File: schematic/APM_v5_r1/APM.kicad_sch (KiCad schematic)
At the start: 27 parts, among them J10 Conn_02x17_Counter_Clockwise, J13 Conn_01x06, J14 POT_FFC, J18 CTRL_FFC, J2 CAN, J20 FPGA_UART, J4 LCD_display, J6 Conn_02x10_Counter_Clockwise, J8 Conn_02x15_Counter_Clockwise, J9 Conn_02x08_Counter_Clockwise

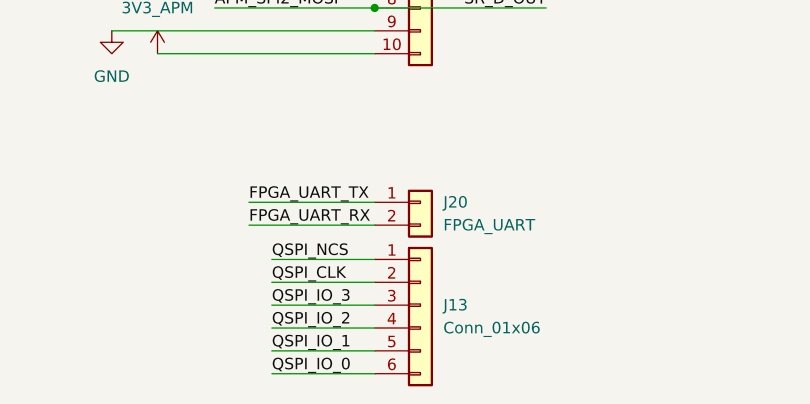
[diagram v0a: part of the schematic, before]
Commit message: figuring out FFC traces next
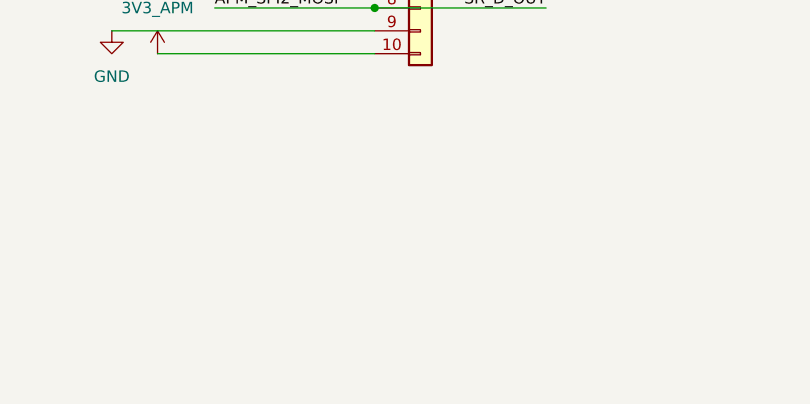
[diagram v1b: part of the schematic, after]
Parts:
- removed J13: Conn_01x06, Connector_PinHeader_2.54mm:PinHeader_1x06_P2.54mm_Vertical, symbol Connector_Generic:Conn_01x06
- removed J20: FPGA_UART, Connector_PinHeader_2.54mm:PinHeader_1x02_P2.54mm_Vertical, symbol Connector_Generic:Conn_01x02

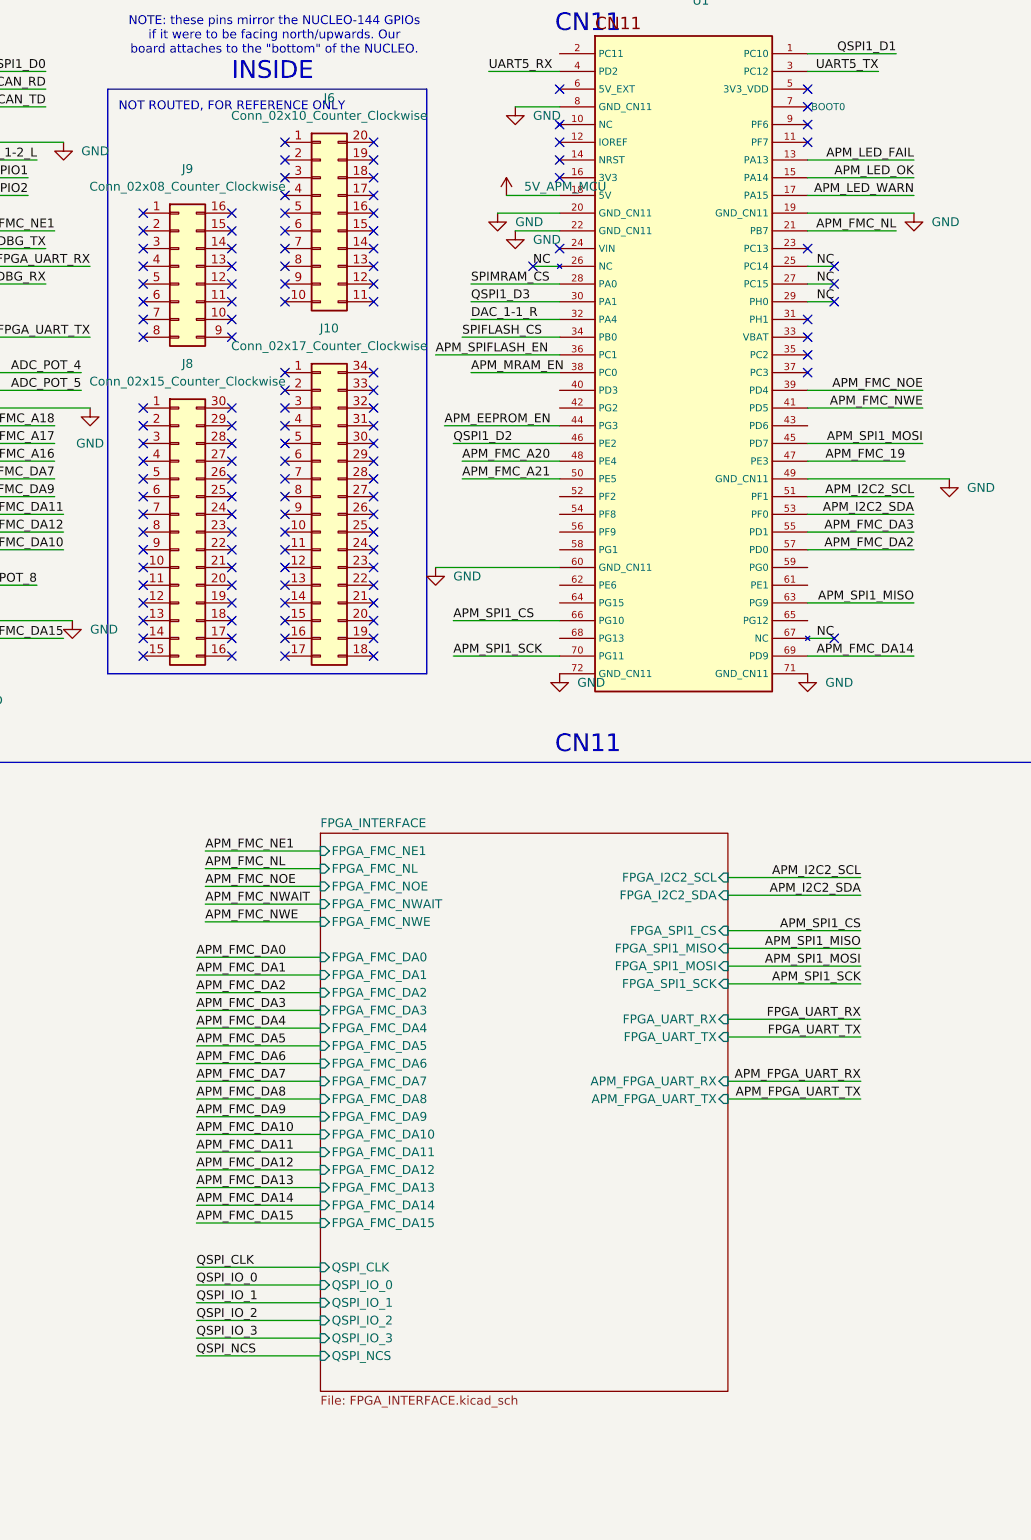
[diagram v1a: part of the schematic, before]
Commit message: getting ACM and APM schematics put together. tool for FMC pin mapping verif
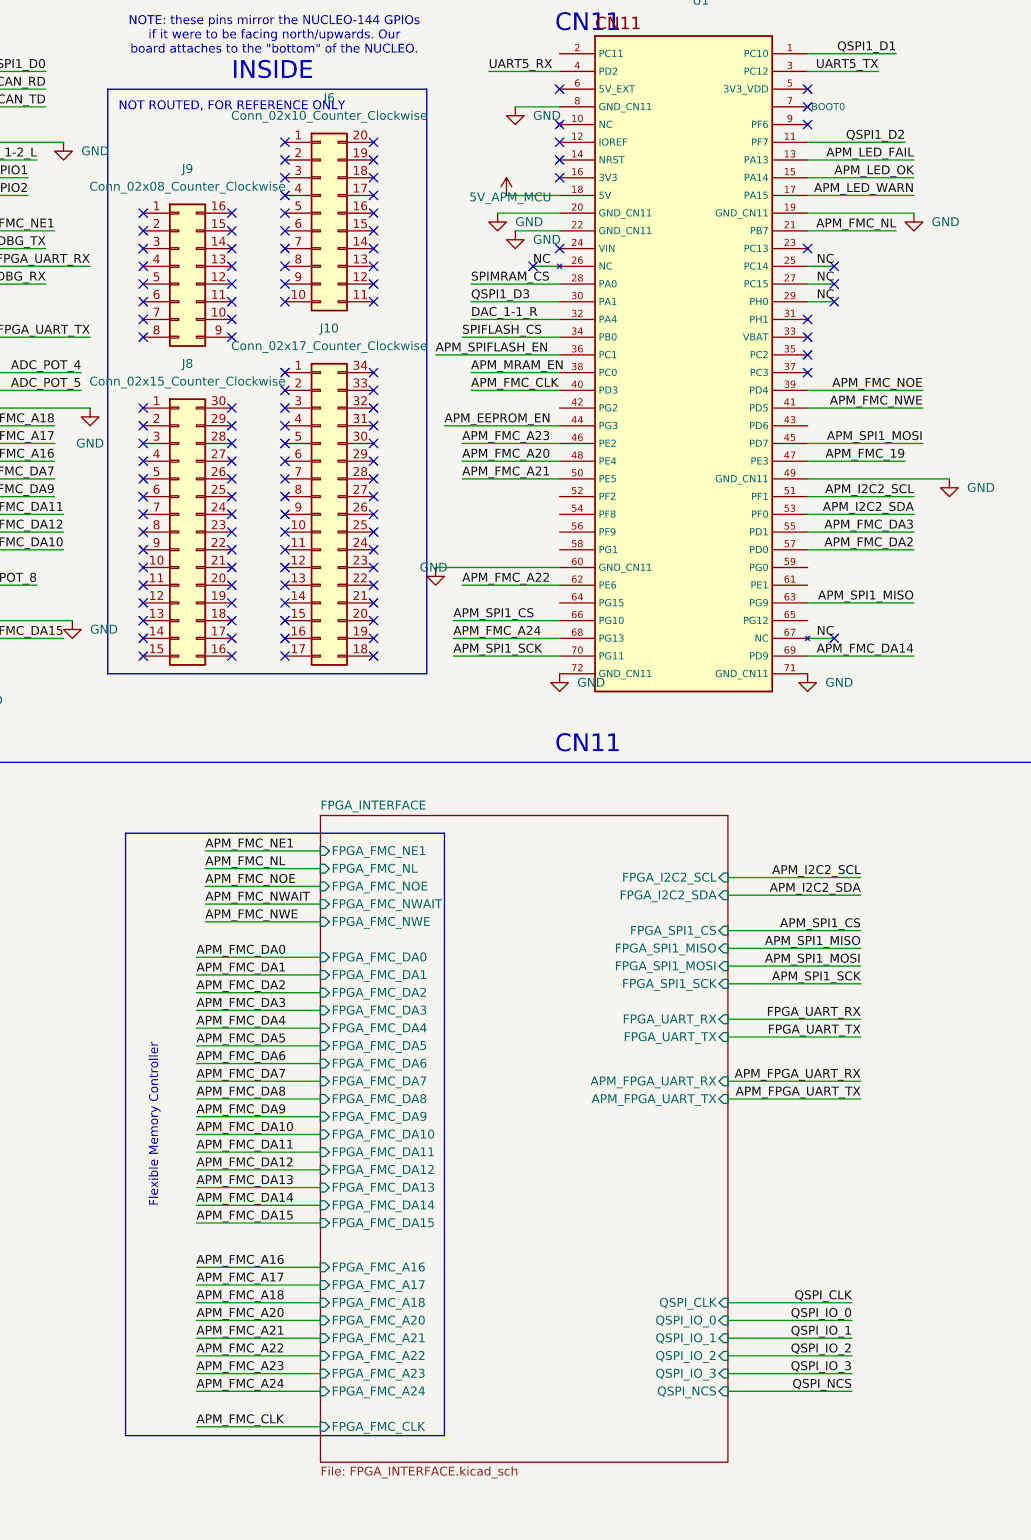
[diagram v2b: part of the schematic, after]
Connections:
- net QSPI1_D2: now also U1.11 (PF7); no longer U1.46 (PE2)
- net APM_FMC_CLK: now reaches U1.40 (PD3)
- net APM_FMC_A22: now reaches U1.62 (PE6)
- net APM_FMC_A24: now reaches U1.68 (PG13)
- new net APM_FMC_A23: U1.46 (PE2)
- no-connect marks 129 -> 128
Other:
- sheet FPGA_INTERFACE ports: added FPGA_FMC_A16, FPGA_FMC_A17, FPGA_FMC_A18, FPGA_FMC_A20, FPGA_FMC_A21, FPGA_FMC_A22, FPGA_FMC_A23, FPGA_FMC_A24, FPGA_FMC_CLK; removed none
- note added: "Flexible Memory Controller"

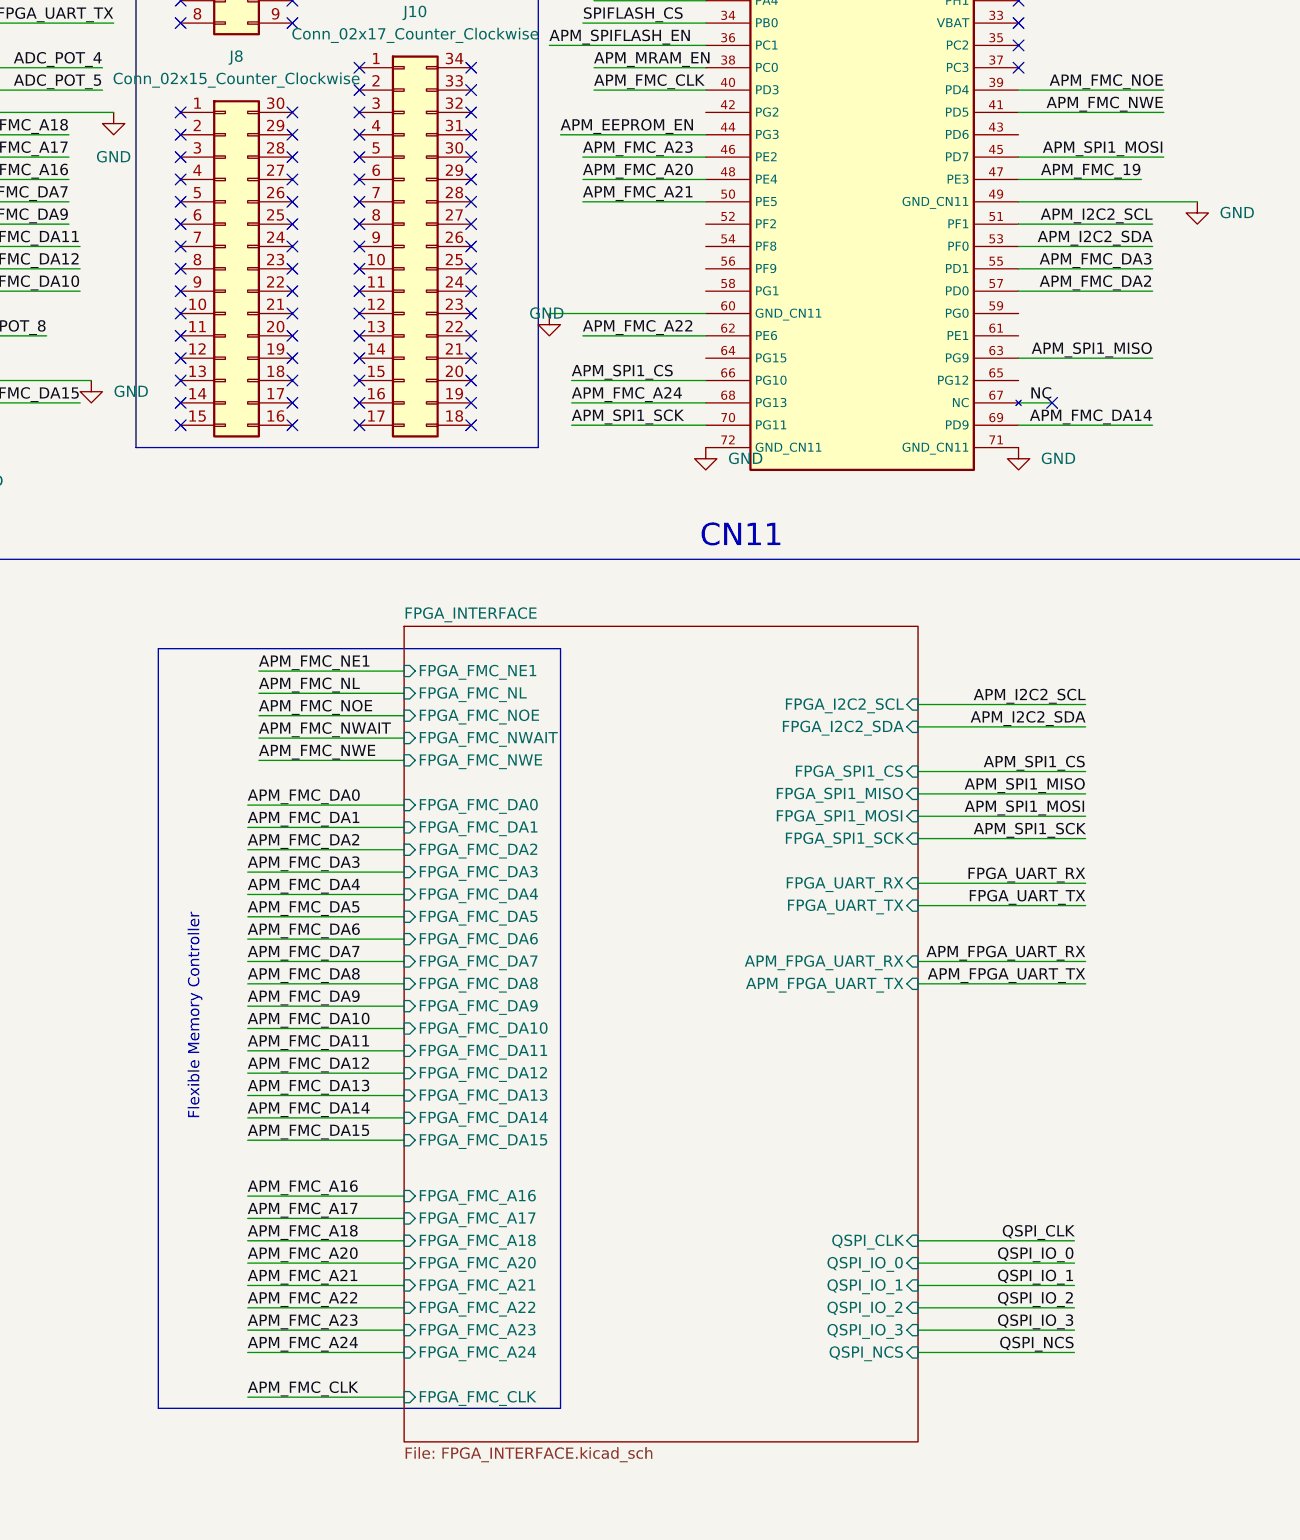
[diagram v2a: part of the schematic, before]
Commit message: adding renders and render script
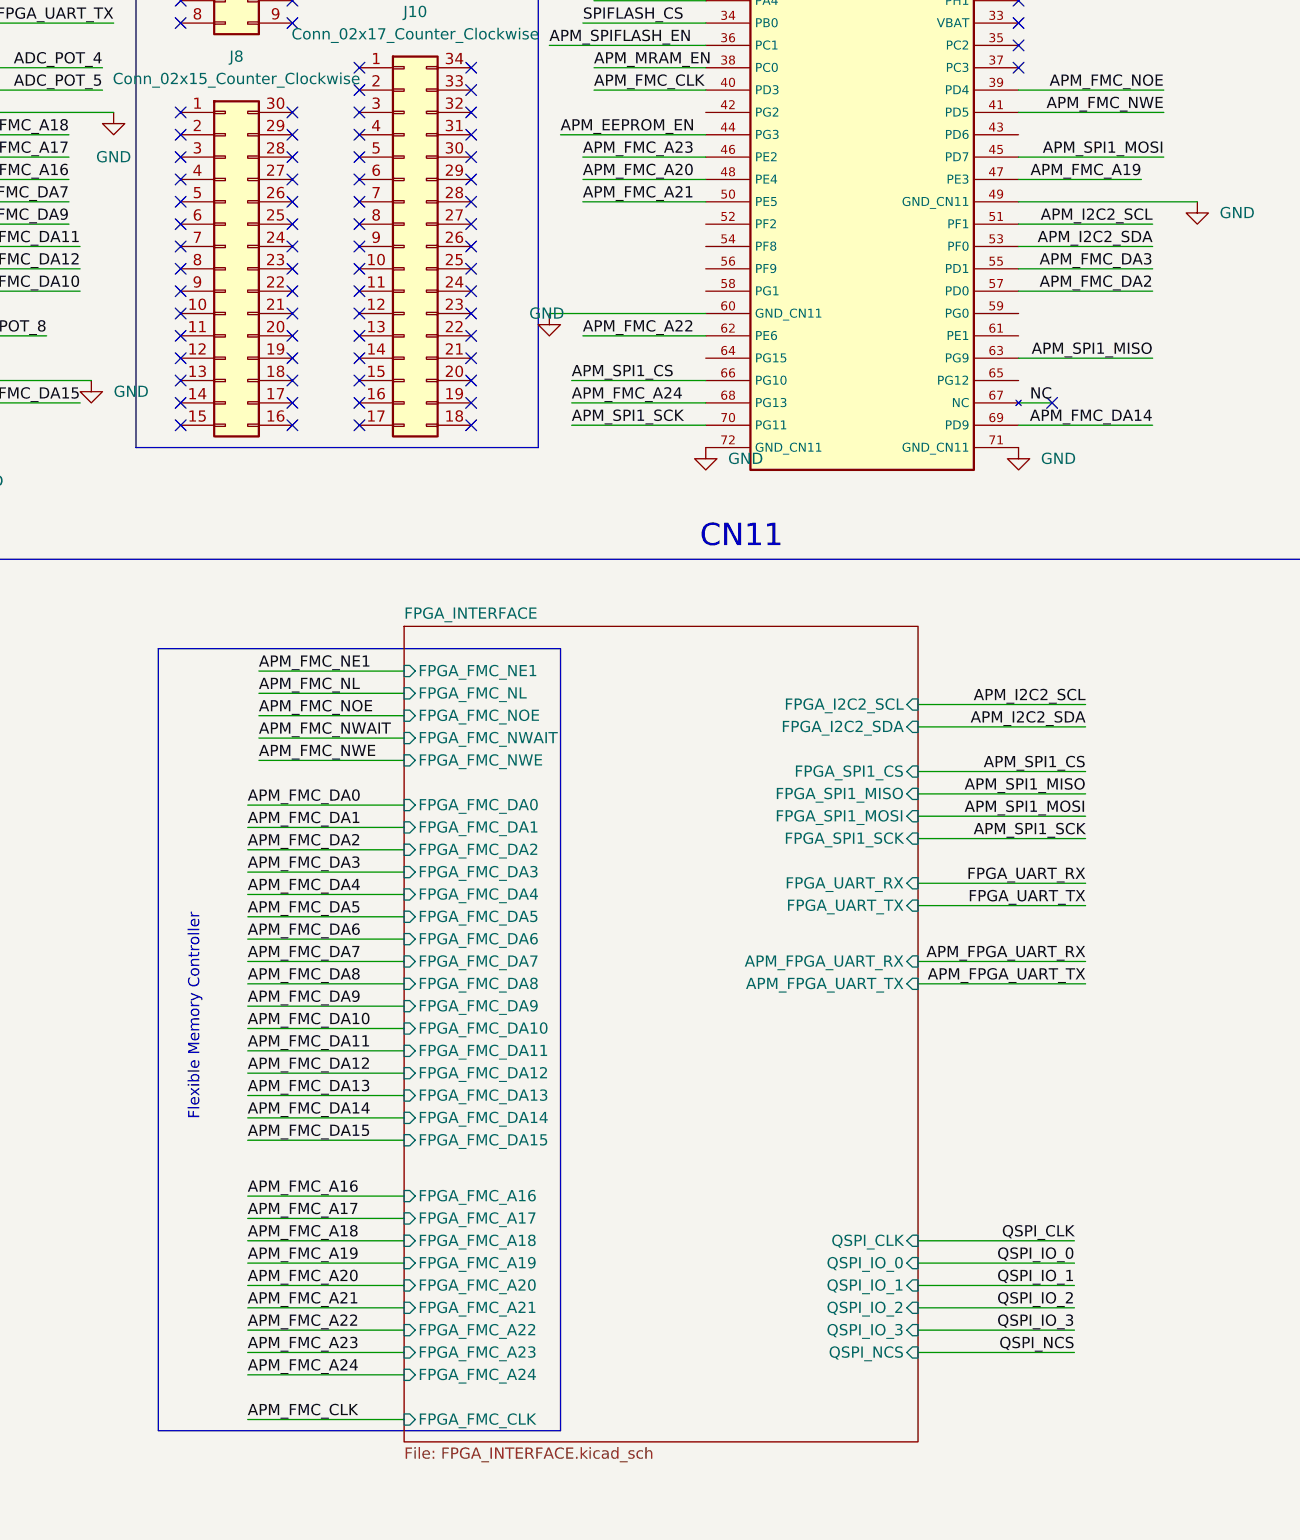
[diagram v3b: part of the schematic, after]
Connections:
- net APM_FMC_19 renamed APM_FMC_A19
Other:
- sheet FPGA_INTERFACE ports: added FPGA_FMC_A19; removed none
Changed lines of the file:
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@@
 	(rectangle
 		(start 248.92 135.89)
-		(end 294.64 222.25)
+		(end 294.64 224.79)
 		(stroke
 			(width 0)
@@
 	(wire
 		(pts
+			(xy 259.08 205.74) (xy 276.86 205.74)
+		)
+		(stroke
+			(width 0)
+			(type default)
+		)
+	)
+	(wire
+		(pts
 			(xy 62.23 234.95) (xy 77.47 234.95)
 		)
@@
 	(wire
 		(pts
-			(xy 259.08 215.9) (xy 276.86 215.9)
+			(xy 259.08 218.44) (xy 276.86 218.44)
 		)
 		(stroke
@@
 	(wire
 		(pts
-			(xy 259.08 210.82) (xy 276.86 210.82)
+			(xy 259.08 213.36) (xy 276.86 213.36)
 		)
 		(stroke
@@
 	(wire
 		(pts
-			(xy 259.08 220.98) (xy 276.86 220.98)
+			(xy 259.08 223.52) (xy 276.86 223.52)
 		)
 		(stroke
@@
 	(wire
 		(pts
-			(xy 259.08 208.28) (xy 276.86 208.28)
+			(xy 259.08 210.82) (xy 276.86 210.82)
 		)
 		(stroke
@@
 	(wire
 		(pts
-			(xy 259.08 205.74) (xy 276.86 205.74)
+			(xy 259.08 208.28) (xy 276.86 208.28)
 		)
 		(stroke
@@
 	(wire
 		(pts
-			(xy 259.08 213.36) (xy 276.86 213.36)
+			(xy 259.08 215.9) (xy 276.86 215.9)
 		)
 		(stroke
@@
 	)
 	(label "APM_FMC_A24"
-		(at 259.08 215.9 0)
+		(at 259.08 218.44 0)
 		(effects
 			(font
@@
 	)
 	(label "APM_FMC_A21"
-		(at 259.08 208.28 0)
+		(at 259.08 210.82 0)
 		(effects
 			(font
@@
 	)
 	(label "APM_FMC_CLK"
-		(at 259.08 220.98 0)
+		(at 259.08 223.52 0)
 		(effects
 			(font
@@
 	)
 	(label "APM_FMC_A23"
-		(at 259.08 213.36 0)
+		(at 259.08 215.9 0)
 		(effects
 			(font
@@
 		)
 	)
+	(label "APM_FMC_A19"
+		(at 259.08 205.74 0)
+		(effects
+			(font
+				(size 1.27 1.27)
+			)
+			(justify left bottom)
+		)
+	)
 	(label "APM_FMC_NWE"
 		(at 260.35 148.59 0)
@@
 	)
 	(label "APM_FMC_A22"
-		(at 259.08 210.82 0)
+		(at 259.08 213.36 0)
 		(effects
 			(font
@@
 	)
 	(label "APM_FMC_A20"
-		(at 259.08 205.74 0)
+		(at 259.08 208.28 0)
 		(effects
 			(font
@@
 		)
 	)
-	(label "APM_FMC_19"
+	(label "APM_FMC_A19"
 		(at 360.68 82.55 180)
 		(effects
@@
 		)
 		(pin "FPGA_FMC_A20" input
-			(at 276.86 205.74 180)
+			(at 276.86 208.28 180)
 			(effects
 				(font
@@
 		)
 		(pin "FPGA_FMC_A21" input
-			(at 276.86 208.28 180)
+			(at 276.86 210.82 180)
 			(effects
 				(font
@@
 		)
 		(pin "FPGA_FMC_A22" input
-			(at 276.86 210.82 180)
+			(at 276.86 213.36 180)
 			(effects
 				(font
@@
 		)
 		(pin "FPGA_FMC_A23" input
-			(at 276.86 213.36 180)
+			(at 276.86 215.9 180)
 			(effects
 				(font
@@
 		)
 		(pin "FPGA_FMC_A24" input
-			(at 276.86 215.9 180)
+			(at 276.86 218.44 180)
 			(effects
 				(font
@@
 		)
 		(pin "FPGA_FMC_CLK" input
-			(at 276.86 220.98 180)
+			(at 276.86 223.52 180)
+			(effects
+				(font
+					(size 1.27 1.27)
+				)
+				(justify left)
+			)
+		)
+		(pin "FPGA_FMC_A19" input
+			(at 276.86 205.74 180)
 			(effects
 				(font

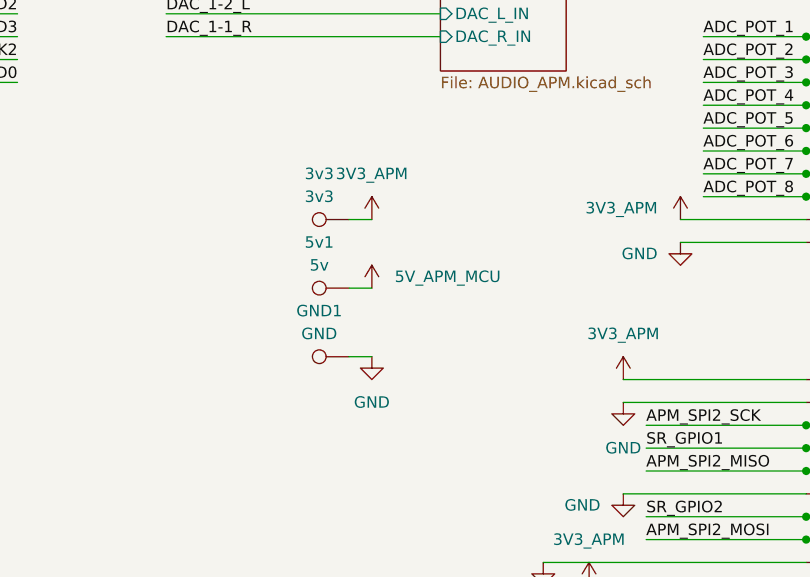
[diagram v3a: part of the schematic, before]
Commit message: schematic for the oscillator board
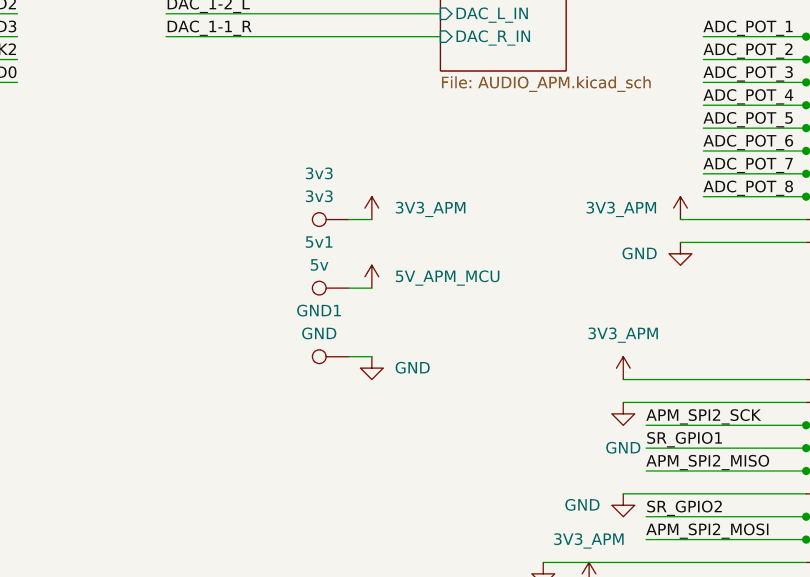
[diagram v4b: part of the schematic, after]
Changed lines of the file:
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@@
 		)
 		(property "Value" "3V3_APM"
-			(at 154.94 157.48 0)
-			(show_name no)
-			(do_not_autoplace no)
-			(effects
-				(font
-					(size 1.27 1.27)
-				)
+			(at 157.48 161.2899 0)
+			(show_name no)
+			(do_not_autoplace no)
+			(effects
+				(font
+					(size 1.27 1.27)
+				)
+				(justify left)
 			)
 		)
@@
 		)
 		(property "Value" "GND"
-			(at 154.94 182.88 0)
-			(show_name no)
-			(do_not_autoplace no)
-			(effects
-				(font
-					(size 1.27 1.27)
-				)
-			)
-		)
+			(at 157.48 179.0699 0)
+			(show_name no)
+			(do_not_autoplace no)
+			(effects
+				(font
+					(size 1.27 1.27)
+				)
+				(justify left)
+			)
+		)
